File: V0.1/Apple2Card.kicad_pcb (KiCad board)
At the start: 2 copper layers, 213.5 x 79.1 mm, 62 parts, among them J1 Conn_01x08_Pin, P2 Conn_02x13_Top_Bottom, SW1 SW_DIP_x08, U1C1 74LS240, U1E1 74LS14, U2 74LS133, U2B1 74LS08, U2D1 74LS138, U2E1 74LS09, U3A1 2764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

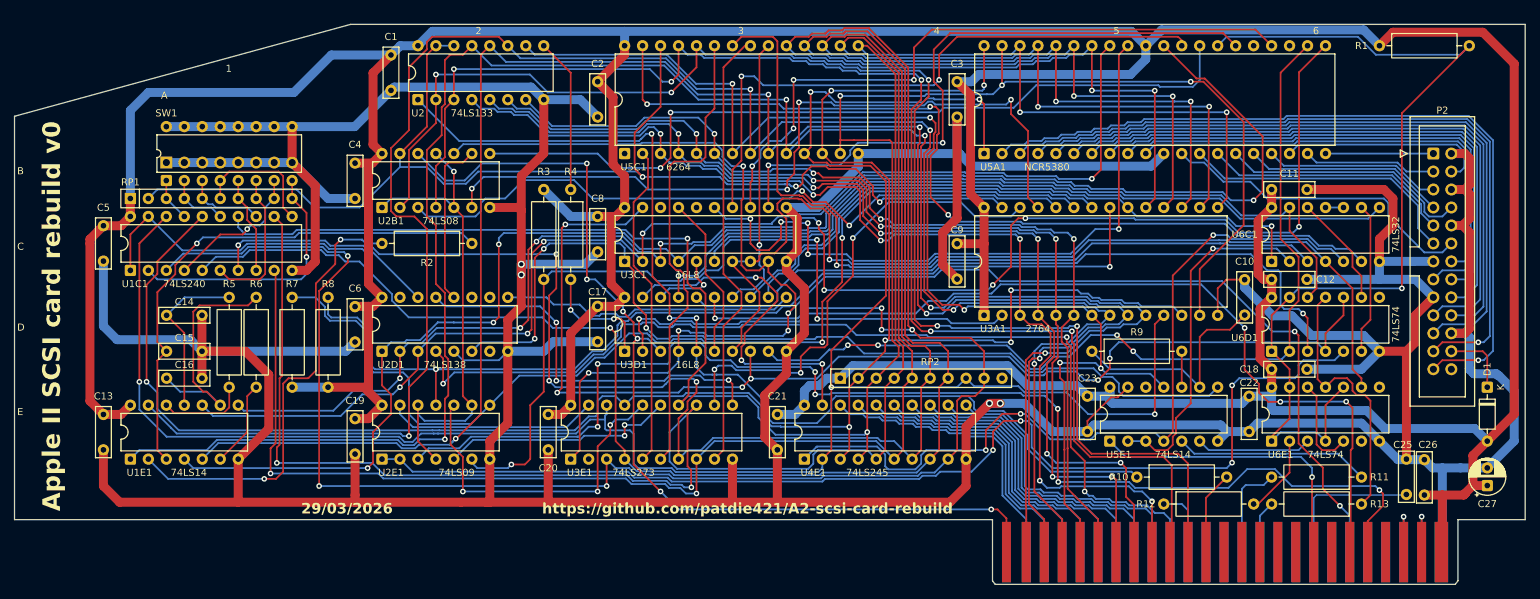
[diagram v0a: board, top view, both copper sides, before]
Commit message: update to remove 74LS09
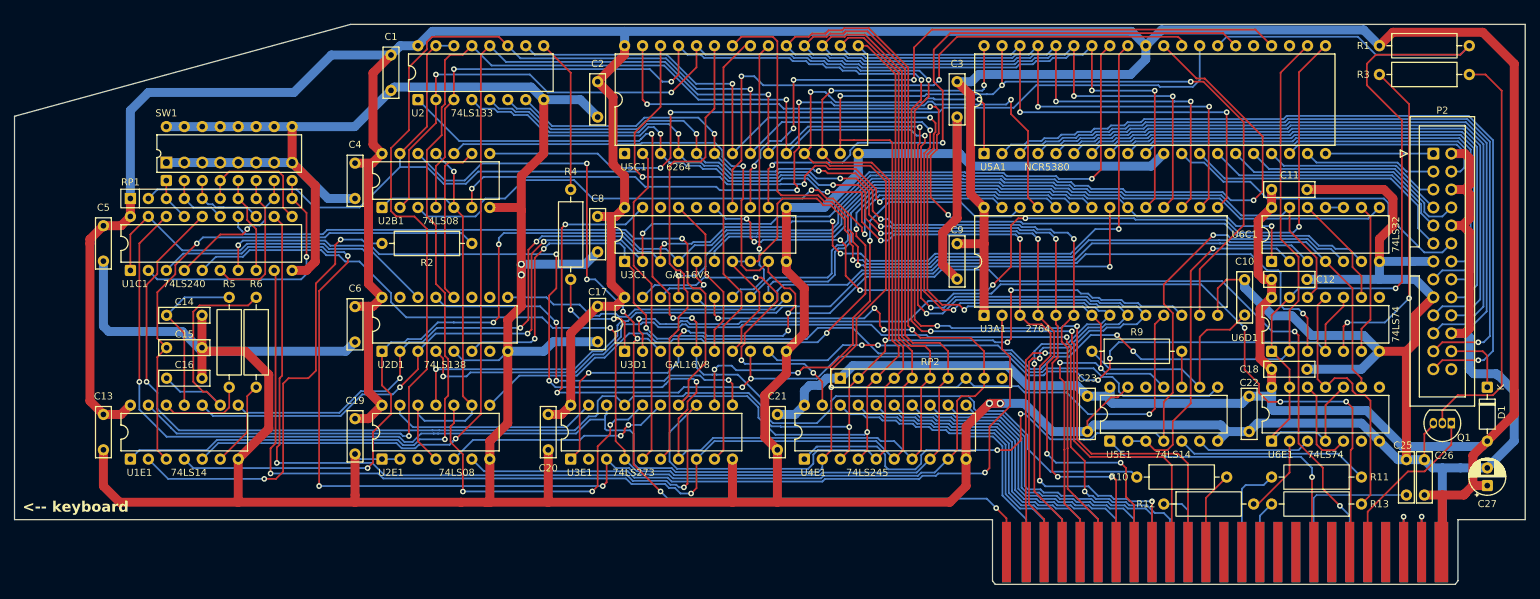
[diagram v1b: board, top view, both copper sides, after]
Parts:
- removed R7, R8: 2k, Resistor_THT:R_Axial_DIN0309_L9.0mm_D3.2mm_P12.70mm_Horizontal
- added Q1: BS170, Package_TO_SOT_THT:TO-92_Inline, F.Cu at (289.6, 86.4)
- R3: value 2k -> 1k
- U2E1: value 74LS09 -> 74LS08
- U3C1, U3D1: value 16L8 -> GAL16V8
- moved R3 134.0 mm to (292.1, 37.1), turned to 180 degrees
- moved C15 0.51 mm to (108.0, 75.7)
- moved C25 0.08 mm to (283.2, 91.5)
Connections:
- R3 pad 1: EA12 -> Net-(Q1-G)
- R3 pad 2: +5V -> Net-(U6D1A-Q)
- U2E1 pad 1: Net-(U6D1A-Q) -> GND
- U2E1 pad 2: Net-(U6D1A-Q) -> GND
- U2E1 pad 3: RDY -> unconnected-(U2E1-Pad3)
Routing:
- net RDY: track 178.6 -> 24.5 mm, vias 7 -> 0
- net Net-(U6D1A-Q): track 160.9 -> 48.0 mm, vias 4 -> 2
- net Net-(Q1-G): track 0.00 -> 58.9 mm
- net EA11: track 148.9 -> 106.0 mm
- net EA10: track 140.3 -> 115.6 mm
- net +5V: track 704.4 -> 684.8 mm
- net EA12: track 117.4 -> 99.0 mm, vias 3 -> 1
- net GND: track 887.7 -> 899.3 mm
- net Net-(U5A1-EOP): track 133.1 -> 143.7 mm
- net Net-(U3C1-IO5): track 135.7 -> 127.4 mm
- net EA9: track 99.5 -> 103.0 mm
- net Net-(U3C1-I7): track 138.7 -> 135.6 mm
- net Net-(U3A1-~{CE}): track 89.5 -> 91.9 mm
- net Net-(U3A1-~{OE}): track 56.3 -> 58.4 mm
- net Net-(U4E1-A->B): track 113.7 -> 115.3 mm
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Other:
- board text added: "<-- keyboard"
- board text removed: "1"
- board text removed: "2"
- board text removed: "29/03/2026"
- board text removed: "3"
- board text removed: "4"
- board text removed: "5"
- board text removed: "6"
- board text removed: "A"
- board text removed: "Apple II SCSI card rebuild v0"
- board text removed: "B"
- board text removed: "C"
- board text removed: "D"
- board text removed: "E"
- board text removed: "https://github.com/patdie421/A2-scsi-card-rebuild"

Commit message: BS170 to 2N3904
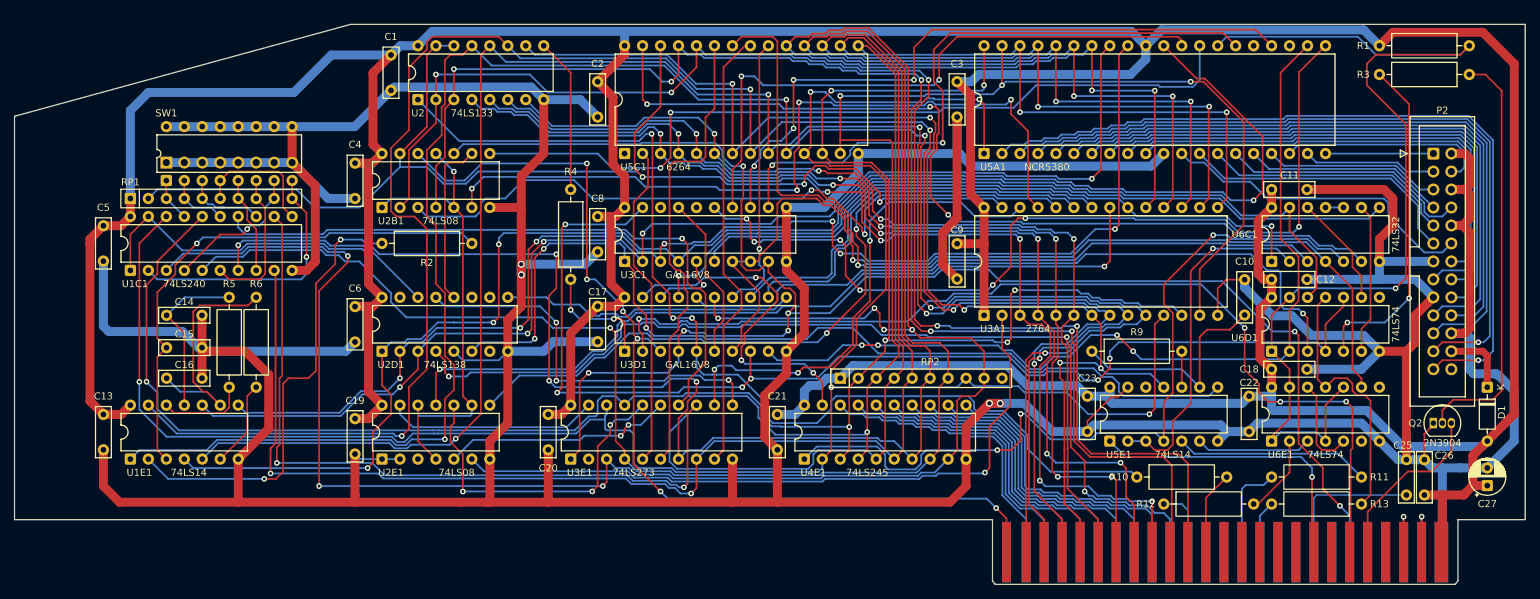
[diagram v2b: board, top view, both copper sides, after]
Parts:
- removed Q1: BS170, Package_TO_SOT_THT:TO-92_Inline
- added Q2: 2N3904, Package_TO_SOT_THT:TO-92_Inline, F.Cu at (287.0, 86.4)
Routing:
- net EA10: track 115.6 -> 114.8 mm
- net A0: track 287.4 -> 288.1 mm
- net RDY: track 24.5 -> 25.1 mm
- net A2: track 281.3 -> 280.7 mm
- net Net-(U2B1-Pad1): track 68.5 -> 67.9 mm
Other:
- board text removed: "<-- keyboard"

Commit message: menage
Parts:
- R3: value 1k -> 10k
- U3C1, U3D1: value GAL16V8 -> ATF16V8C
- U3E1: value 74LS273 -> 74LS273/74HCT273
- moved C20 0.64 mm to (161.3, 85.2)
- moved C22 0.63 mm to (260.4, 82.5)
- moved Q2 0.51 mm to (287.0, 86.9)
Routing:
- net GND: track 899.3 -> 901.1 mm
- net d3: track 288.5 -> 287.3 mm
- net EA8: track 110.6 -> 109.4 mm
- net d4: track 269.2 -> 268.0 mm
- net d7: track 355.6 -> 354.6 mm
- net d5: track 287.2 -> 286.5 mm
- net d6: track 284.4 -> 283.8 mm
- net RDY: track 25.1 -> 24.6 mm
- net Net-(Q2-B): track 59.3 -> 59.8 mm
